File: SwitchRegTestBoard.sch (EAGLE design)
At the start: 17 parts

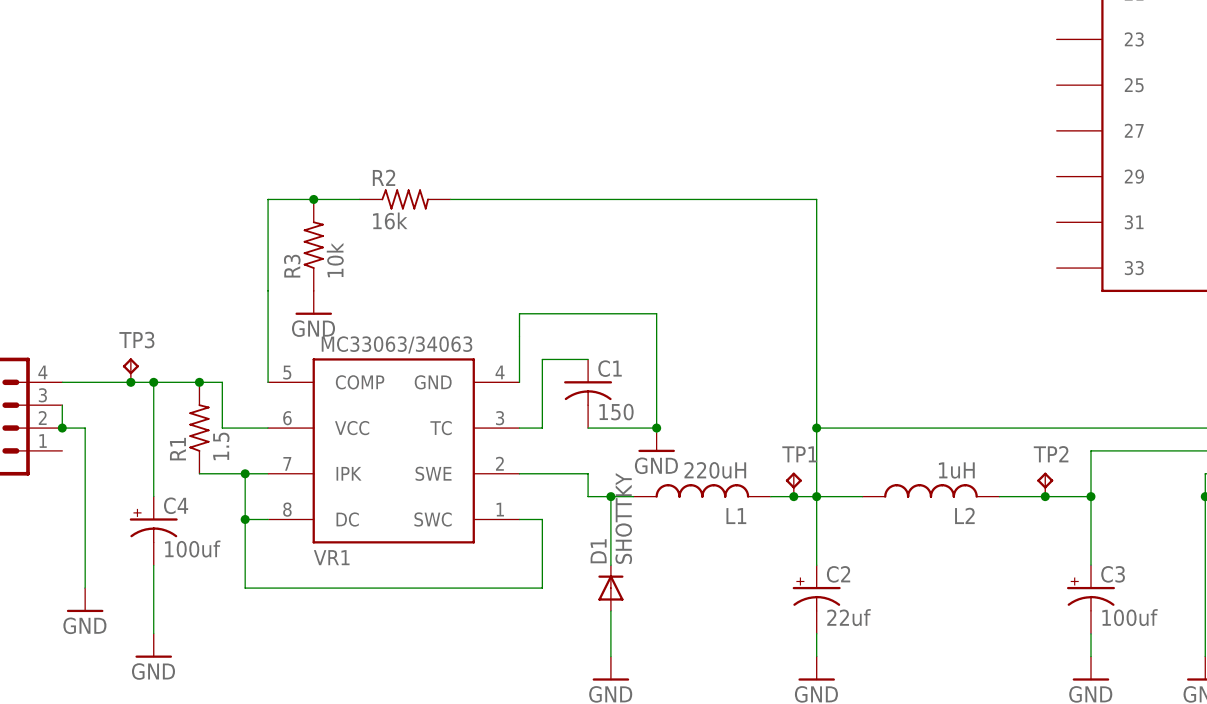
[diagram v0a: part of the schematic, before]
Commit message: star ground around switcher.  Additional resistor pad for low side of divider for tweaking resistance
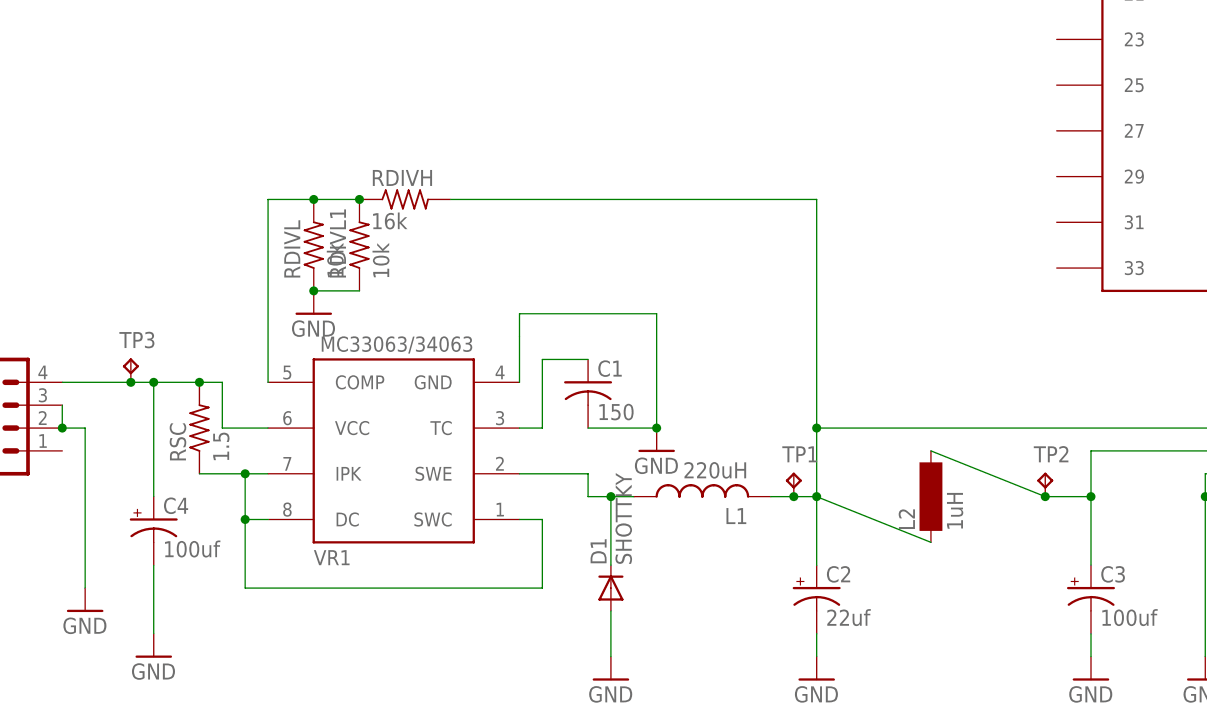
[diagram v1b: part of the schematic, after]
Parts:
- added RDIVL1: 10k, LL:R-US_R0805
- L2: device LL:L-USL0707MM -> inductor-neosid:SM-NE29
- renumbered R1 to RSC, R2 to RDIVH, R3 to RDIVL
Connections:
- removed net N$6: RDIVH.1, RDIVL.2, VR1.COMP
- new net DIVIDERCENTER: RDIVH.1, RDIVL.2, RDIVL1.2, VR1.COMP
- net GND: now also RDIVL1.1
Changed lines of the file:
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@@
 <part name="GND2" library="supply1" deviceset="GND" device=""/>
 <part name="GND3" library="supply1" deviceset="GND" device=""/>
-<part name="R1" library="LL" deviceset="R-US_" device="R1206" value="1.5"/>
-<part name="R2" library="LL" deviceset="R-US_" device="R0805" value="16k"/>
-<part name="R3" library="LL" deviceset="R-US_" device="R0805" value="10k"/>
+<part name="RSC" library="LL" deviceset="R-US_" device="R1206" value="1.5"/>
+<part name="RDIVH" library="LL" deviceset="R-US_" device="R0805" value="16k"/>
+<part name="RDIVL" library="LL" deviceset="R-US_" device="R0805" value="10k"/>
 <part name="GND4" library="supply1" deviceset="GND" device=""/>
 <part name="C2" library="LL" deviceset="CPOL-US" device="C" value="22uf"/>
-<part name="L2" library="LL" deviceset="L-US" device="L0707MM" value="1uH"/>
+<part name="L2" library="inductor-neosid" deviceset="SM-NE29" device="" value="1uH"/>
 <part name="C3" library="LL" deviceset="CPOL-US" device="C" value="100uf"/>
 <part name="GND5" library="supply1" deviceset="GND" device=""/>
@@
 <part name="TP2" library="testpad" deviceset="TP" device="TP10R"/>
 <part name="TP3" library="testpad" deviceset="TP" device="TP10R"/>
+<part name="RDIVL1" library="LL" deviceset="R-US_" device="R0805" value="10k"/>
 </parts>
 <sheets>
@@
 <instance part="GND2" gate="1" x="104.14" y="17.78"/>
 <instance part="GND3" gate="1" x="22.86" y="25.4"/>
-<instance part="R1" gate="G$1" x="35.56" y="45.72" rot="R90"/>
-<instance part="R2" gate="G$1" x="58.42" y="71.12"/>
-<instance part="R3" gate="G$1" x="48.26" y="66.04" rot="R90"/>
+<instance part="RSC" gate="G$1" x="35.56" y="45.72" rot="R90"/>
+<instance part="RDIVH" gate="G$1" x="58.42" y="71.12"/>
+<instance part="RDIVL" gate="G$1" x="48.26" y="66.04" rot="R90"/>
 <instance part="GND4" gate="1" x="48.26" y="58.42"/>
 <instance part="C2" gate="G$1" x="104.14" y="27.94"/>
@@
 <instance part="TP2" gate="G$1" x="129.54" y="40.64"/>
 <instance part="TP3" gate="G$1" x="27.94" y="53.34"/>
+<instance part="RDIVL1" gate="G$1" x="53.34" y="66.04" rot="R90"/>
 </instances>
 <busses>
@@
 <junction x="40.64" y="40.64"/>
 <junction x="40.64" y="35.56"/>
-<pinref part="R1" gate="G$1" pin="1"/>
+<pinref part="RSC" gate="G$1" pin="1"/>
 <pinref part="VR1" gate="G$1" pin="IPK"/>
 <pinref part="VR1" gate="G$1" pin="DC"/>
@@
 </segment>
 <segment>
-<pinref part="R3" gate="G$1" pin="1"/>
+<pinref part="RDIVL" gate="G$1" pin="1"/>
 <pinref part="GND4" gate="1" pin="GND"/>
+<pinref part="RDIVL1" gate="G$1" pin="1"/>
+<wire x1="48.26" y1="60.96" x2="53.34" y2="60.96" width="0.1524" layer="91"/>
+<junction x="48.26" y="60.96"/>
 </segment>
 <segment>
@@
 <junction x="30.48" y="50.8"/>
 <pinref part="VR1" gate="G$1" pin="VCC"/>
-<pinref part="R1" gate="G$1" pin="2"/>
+<pinref part="RSC" gate="G$1" pin="2"/>
 <pinref part="JP1" gate="G$1" pin="4"/>
 <pinref part="C4" gate="G$1" pin="+"/>
@@
 </segment>
 </net>
-<net name="N$6" class="0">
-<segment>
-<wire x1="43.18" y1="50.8" x2="43.18" y2="60.96" width="0.1524" layer="91"/>
-<wire x1="43.18" y1="60.96" x2="43.18" y2="71.12" width="0.1524" layer="91"/>
+<net name="DIVIDERCENTER" class="0">
+<segment>
+<wire x1="43.18" y1="50.8" x2="43.18" y2="71.12" width="0.1524" layer="91"/>
 <wire x1="43.18" y1="71.12" x2="48.26" y2="71.12" width="0.1524" layer="91"/>
 <wire x1="48.26" y1="71.12" x2="53.34" y2="71.12" width="0.1524" layer="91"/>
 <junction x="48.26" y="71.12"/>
 <pinref part="VR1" gate="G$1" pin="COMP"/>
-<pinref part="R3" gate="G$1" pin="2"/>
-<pinref part="R2" gate="G$1" pin="1"/>
+<pinref part="RDIVL" gate="G$1" pin="2"/>
+<pinref part="RDIVH" gate="G$1" pin="1"/>
+<pinref part="RDIVL1" gate="G$1" pin="2"/>
+<junction x="53.34" y="71.12"/>
 </segment>
 </net>
@@
 <wire x1="134.62" y1="30.48" x2="134.62" y2="38.1" width="0.1524" layer="91"/>
 <wire x1="134.62" y1="38.1" x2="129.54" y2="38.1" width="0.1524" layer="91"/>
-<wire x1="129.54" y1="38.1" x2="124.46" y2="38.1" width="0.1524" layer="91"/>
+<wire x1="129.54" y1="38.1" x2="116.84" y2="43.18" width="0.1524" layer="91"/>
 <wire x1="134.62" y1="38.1" x2="134.62" y2="43.18" width="0.1524" layer="91"/>
 <wire x1="134.62" y1="43.18" x2="149.86" y2="43.18" width="0.1524" layer="91"/>
@@
 <wire x1="99.06" y1="38.1" x2="101.6" y2="38.1" width="0.1524" layer="91"/>
 <wire x1="101.6" y1="38.1" x2="104.14" y2="38.1" width="0.1524" layer="91"/>
-<wire x1="104.14" y1="38.1" x2="109.22" y2="38.1" width="0.1524" layer="91"/>
+<wire x1="104.14" y1="38.1" x2="116.84" y2="33.02" width="0.1524" layer="91"/>
 <wire x1="104.14" y1="71.12" x2="104.14" y2="45.72" width="0.1524" layer="91"/>
 <wire x1="104.14" y1="45.72" x2="104.14" y2="38.1" width="0.1524" layer="91"/>
@@
 <pinref part="L1" gate="G$1" pin="2"/>
 <pinref part="L2" gate="G$1" pin="1"/>
-<pinref part="R2" gate="G$1" pin="2"/>
+<pinref part="RDIVH" gate="G$1" pin="2"/>
 <pinref part="C2" gate="G$1" pin="+"/>
 <pinref part="JP2" gate="G$1" pin="1"/>
